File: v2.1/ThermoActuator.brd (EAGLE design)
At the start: 99.1 x 80 mm, 82 parts, among them IC1 PCF8574T, IC2 ULN2003AD, IC3 REG1117, Q1 200mA/50V, Q2 200mA/50V, U1 CD74HCT4051_D_16

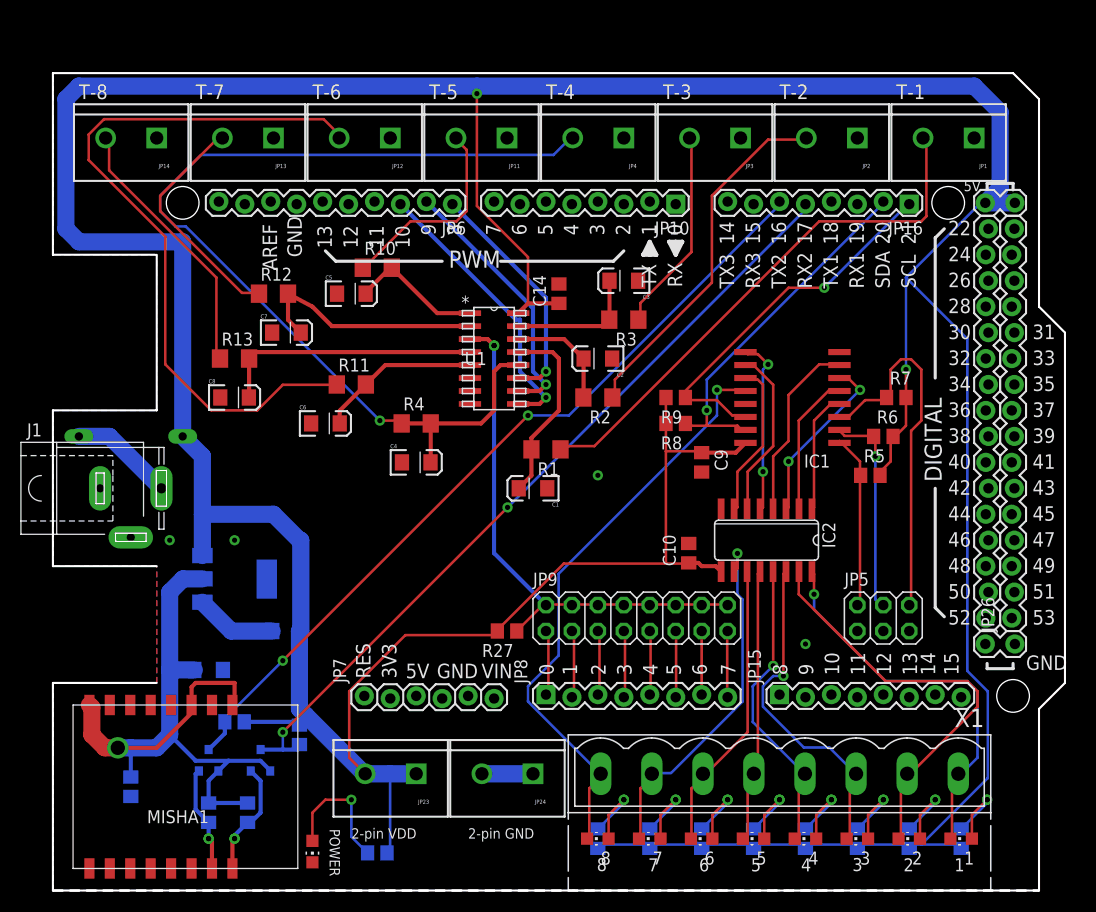
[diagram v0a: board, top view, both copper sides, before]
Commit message: ThermoShield v2.1
a new version with WiFi support and cloud capabilities
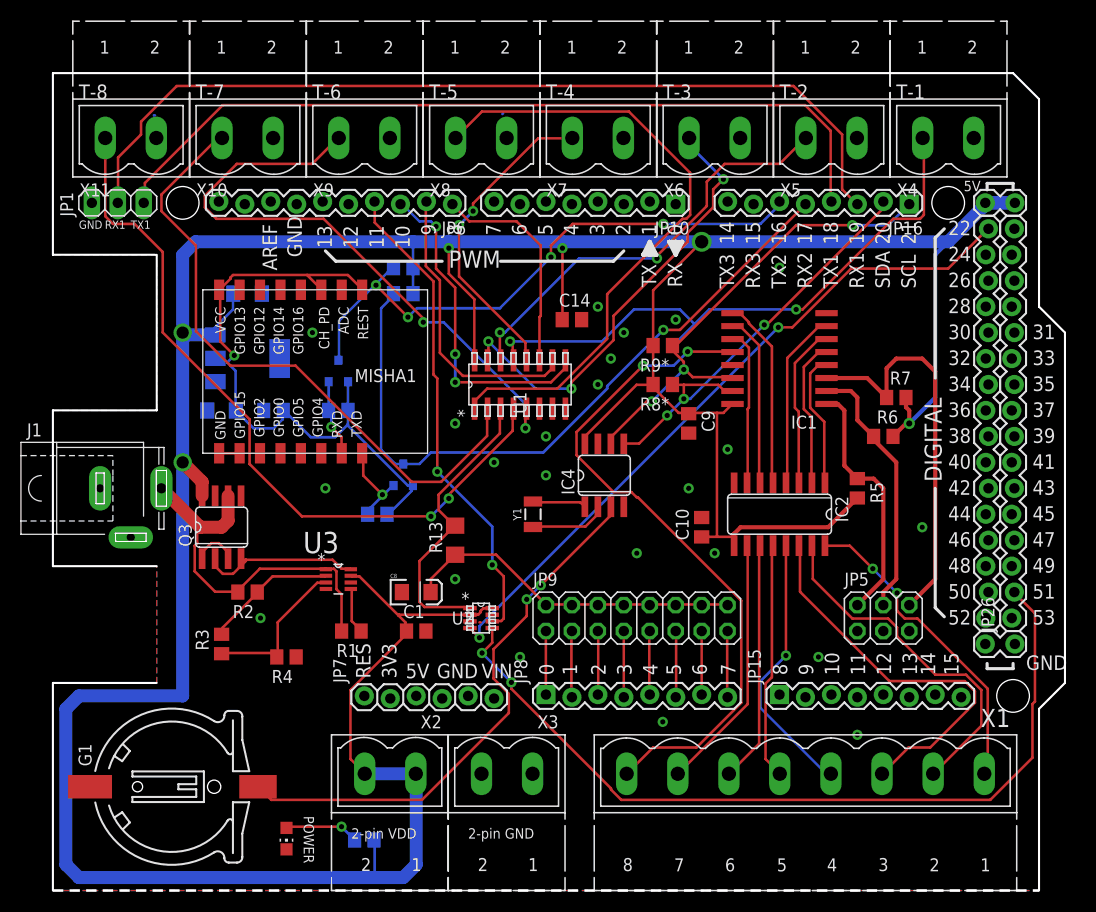
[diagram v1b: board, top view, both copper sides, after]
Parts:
- removed 1, 2, 3, 4, 5, 6, 7, 8: (no value), led:CHIP-LED0805
- removed C2, C3, C4, C5, C6, C7: 5uF, SparkFun-Capacitors:EIA3216
- removed D1: 1N4001, diode:D-10
- removed JP11, JP12, JP13, JP14, JP2, JP23, JP24, JP3, JP4: M025MM, SparkFun-Connectors:SCREWTERMINAL-5MM-2
- removed R10, R11, R12: 1K, rcl:R1206
- removed R14, R15, R16, R17, R18, R19, R20, R21: 3K3, rcl:R0805
- removed R27: 10K, resistor:R0805
- removed R8, R9: 4K7, rcl:R0805
- added G1: CH291-1220LF, battery:CH291-1220LF
- added IC4: DS1307, dallas-1:SOIC-8
- added Q3: MOSFET-NCHANNEL_DUAL, lio:SO08
- added R8*, R9*: 4K7, rcl:R0805
- added U2: AD5165BUJZ100-R2, AD5165_DigitalPot:UJ_8
- added U3: LTC4365CTS8TRMPBF, LTC_By_element14_Batch_1:SOT65P280X100-8N
- added X10, X11, X2, X3, X4, X5, X6, X7, X8, X9: (no value), con-phoenix-500:MSTBV2
- added Y1: (no value), SparkFun-FreqCtrl:CRYSTAL-SMD-3.2X1.5MM
- C1: value 5uF -> 100nF; device SparkFun-Capacitors:EIA3216 -> rcl:C0805
- JP1: value M025MM -> (none); device SparkFun-Connectors:SCREWTERMINAL-5MM-2 -> pinhead:1X03
- R1: value 1K -> 100K; device rcl:R1206 -> rcl:R0805
- R2: value 1K -> 1.82M; device rcl:R1206 -> rcl:R0805
- R3, R4: value 1K -> 150K; device rcl:R1206 -> rcl:R0805
- moved JP1 84.1 mm to (6.35, 67.3)
- moved R3 50.6 mm to (16.5, 24.1), turned to 90 degrees
- moved R26 47.4 mm to (34.3, 61.0)
- moved R25 44.4 mm to (34.3, 58.4), turned to 180 degrees
- moved MISHA1 42.6 mm to (26.7, 50.8)
- moved R24 41.4 mm to (27.9, 47.0), turned to 180 degrees
- moved Q2 40.2 mm to (27.9, 50.8)
- moved C13 39.4 mm to (21.6, 47.0), turned to 0 degrees
- moved R2 39.2 mm to (19.1, 29.2)
- moved C11 33.2 mm to (19.1, 58.4), turned to 0 degrees
- moved R23 31.9 mm to (31.8, 36.8), turned to 180 degrees
- moved Q1 31.2 mm to (34.3, 40.6)
- moved R13 28.0 mm to (39.4, 34.3), turned to 90 degrees
- moved R4 26.2 mm to (22.9, 22.9), turned to 180 degrees
- moved C8 26.1 mm to (35.6, 29.2)
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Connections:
- removed net D51: JP26.2
- removed net D52: JP27.16
- removed net N$16: 4.A, R17.1
- removed net N$17: 5.A, R18.1
- removed net N$18: 6.A, R19.1
- removed net N$19: 7.A, R20.1
- removed net N$23: JP14.2, R13.1
- removed net N$32: 8.A, R21.1
- new net D51(MOSI): JP26.2, U2.5
- new net D52(SCLK): JP27.16, U2.4
- net AO0: no longer 1.C
- net AO1: no longer 2.C
- net AO2: no longer 3.C
- net AO3: no longer 4.C
- net AO4: no longer 5.C
- net AO5: no longer 6.C
- net AO6: no longer 7.C
- net AO7: no longer 8.C
- net AS0: now also X4.1; no longer C1.A, R1.2
- net AS1: now also X5.1; no longer C2.A, R2.2
- net AS2: now also X6.1; no longer C3.A, R3.2
- net AS3: now also X7.1; no longer C4.A, R4.2
- net AS4: now also X8.1; no longer C5.A, R10.2
- net AS5: now also X9.1; no longer C6.A, R11.2
- net AS6: now also X10.1; no longer C7.A, R12.2
- net AS7: now also X11.1; no longer C8.A, R13.2
- net D11: now also U2.6
- net GND: now also C1.2, G1.-, JP1.3, R4.1, U2.3, U3.4, X10.2, X11.2, X3.1, X3.2, X4.2, X5.2, X6.2, X7.2, X8.2, X9.2; no longer C1.C, C2.C, C3.C, C4.C, C5.C, C6.C, C7.C, JP1.1, JP11.1, JP12.1, JP13.1, JP14.1, JP2.1, JP24.1, JP24.2, JP3.1, JP4.1
- net N$1: now also U3.5; no longer JP1.2
- net N$11: now also IC4.4; no longer JP3.2, R3.1
- net N$12: now also R2.1, R3.2, U3.2; no longer JP4.2, R4.1
- net N$13: now also R3.1, R4.2, U3.3; no longer 1.A, R14.1
- net N$14: now also Q3.2, Q3.4, U3.8; no longer 2.A, R15.1
- net N$15: now also Q3.1, Q3.3; no longer 3.A, R16.1
- net N$2: now also R13.2, U1.3, U2.1; no longer JP2.2, R2.1
- net N$20: now also IC4.1, Y1.P$2; no longer JP11.2, R10.1
- net N$21: now also IC4.2, Y1.P$1; no longer JP12.2, R11.1
- net N$22: now also G1.+, IC4.3; no longer JP13.2, R12.1
- net N$36: now also C8.A, R13.1; no longer R27.1, U1.3
- net N$42: now also Q3.6, R1.2, R2.2, U3.1; no longer D1.A
- net RX1: now also JP1.2
- net SCL: now also IC4.6, R9*.1; no longer R9.1
- net SDA: now also IC4.5, R8*.1; no longer R8.1
- net TX1: now also JP1.1
- net VDD: now also C1.1, IC4.8, Q3.8, R8*.2, R9*.2, U2.2, U2.8, U3.7, X2.1, X2.2; no longer D1.C, JP23.1, JP23.2, R14.2, R15.2, R16.2, R17.2, R18.2, R19.2, R20.2, R21.2, R27.2, R8.2, R9.2
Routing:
- net RX1: track 0.00 -> 88.4 mm
- net D51(MOSI): track 0.00 -> 82.0 mm, vias 0 -> 2
- net TX1: track 0.00 -> 80.3 mm
- net VDD: track 451.9 -> 371.9 mm, vias 2 -> 6
- net D52(SCLK): track 0.00 -> 68.4 mm, vias 0 -> 2
- net N$12: track 79.2 -> 13.0 mm, vias 1 -> 0
- net N$21: track 71.4 -> 7.62 mm
- net AS4: track 13.2 -> 62.6 mm
- net N$1: track 53.1 -> 4.56 mm
- net D11: track 0.00 -> 47.3 mm, vias 0 -> 2
- net AS7: track 25.7 -> 72.8 mm, vias 0 -> 2
- net AS5: track 15.8 -> 60.5 mm, vias 0 -> 2
- net AS0: track 18.6 -> 58.8 mm, vias 0 -> 2
- net AS6: track 23.2 -> 62.1 mm
- net AS1: track 11.0 -> 42.1 mm, vias 0 -> 2
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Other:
- board text added: "Thermoshield v2.1 OddCloset (C) 2016"

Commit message: routing complete, LEDs are back
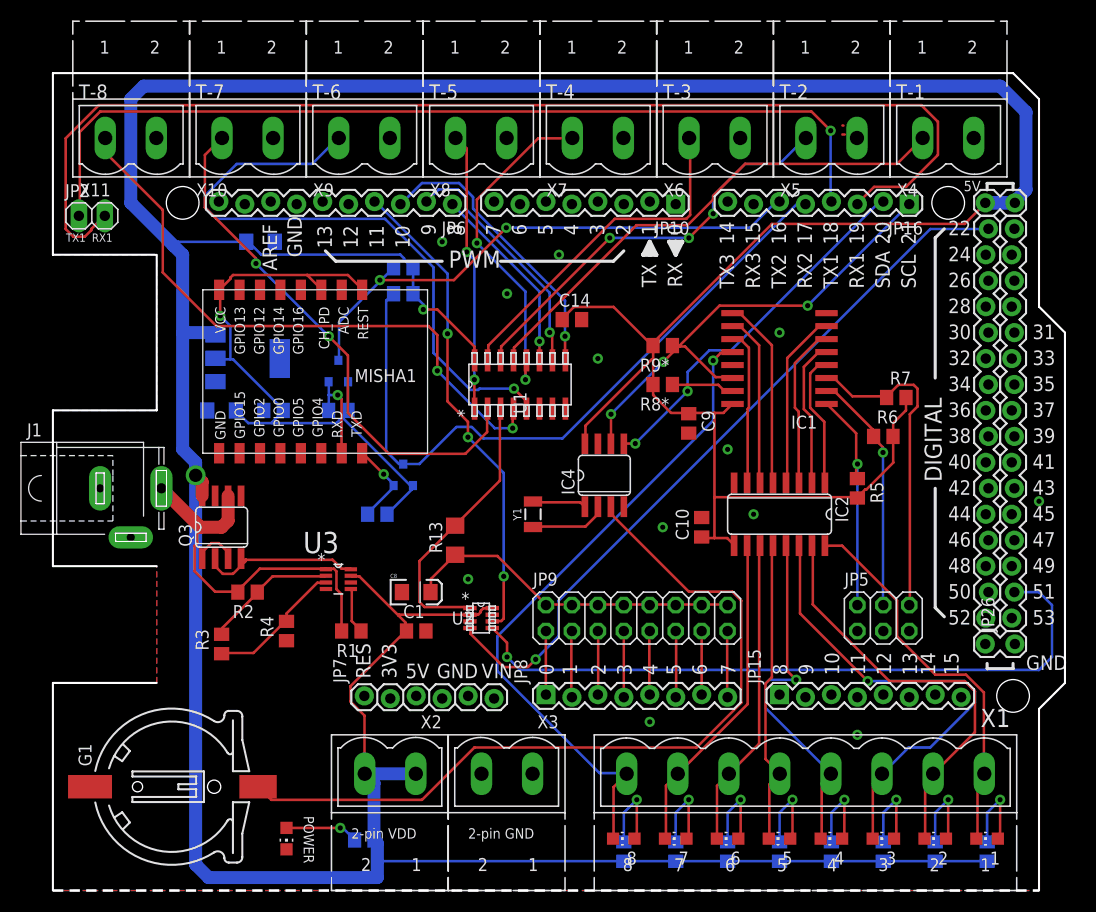
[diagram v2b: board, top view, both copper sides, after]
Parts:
- removed JP1: (no value), pinhead:1X03
- added 1, 2, 3, 4, 5, 6, 7, 8: (no value), led:CHIP-LED0805
- added JP2: (no value), pinhead:1X02
- added R10, R11, R12, R14, R15, R16, R8, R9: 3K3, rcl:R0805
- moved C11 5.24 mm to (20.3, 63.5)
- moved R4 2.54 mm to (22.9, 25.4), turned to 90 degrees
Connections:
- new net N$23: 2.A, R9.1
- new net N$32: 3.A, R10.1
- new net N$46: 4.A, R11.1
- new net N$47: 5.A, R12.1
- new net N$48: 6.A, R14.1
- new net N$49: 7.A, R15.1
- new net N$50: 8.A, R16.1
- net AO0: now also 1.C
- net AO1: now also 2.C
- net AO2: now also 3.C
- net AO3: now also 4.C
- net AO4: now also 5.C
- net AO5: now also 6.C
- net AO6: now also 7.C
- net AO7: now also 8.C
- net GND: now also IC4.4; no longer JP1.3
- net N$11: now also 1.A, R8.1; no longer IC4.4
- net RX1: now also JP2.2; no longer JP1.2
- net TX1: now also JP2.1; no longer JP1.1
- net VDD: now also R10.2, R11.2, R12.2, R14.2, R15.2, R16.2, R8.2, R9.2
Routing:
- net VDD: track 371.9 -> 469.0 mm, vias 6 -> 2
- net AS4: track 62.6 -> 27.3 mm, vias 0 -> 2
- net RX1: track 88.4 -> 114.5 mm
- net N$22: track 54.2 -> 78.7 mm, vias 2 -> 0
- net D51(MOSI): track 82.0 -> 67.1 mm, vias 2 -> 1
- net AS7: track 72.8 -> 60.1 mm
- net AS6: track 62.1 -> 51.9 mm, vias 0 -> 2
- net TX1: track 80.3 -> 90.3 mm, vias 0 -> 1
- net AS2: track 44.0 -> 34.2 mm, vias 3 -> 0
- net AS0: track 58.8 -> 50.0 mm, vias 2 -> 0
- net N$50: track 0.00 -> 8.56 mm, vias 0 -> 1
- net N$49: track 0.00 -> 8.56 mm, vias 0 -> 1
- net N$48: track 0.00 -> 8.56 mm, vias 0 -> 1
- net N$47: track 0.00 -> 8.56 mm, vias 0 -> 1
- net N$46: track 0.00 -> 8.56 mm, vias 0 -> 1
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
